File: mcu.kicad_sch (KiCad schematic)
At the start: 38 parts, among them IC14 W25Q64FWSSIG, IC19 TPS22975, IC3 HDC2080, IC5 CAT25160VI-GT3, J1 JST_PH_3PIN, J3 TC2030-IDC, J4 Conn_01x04, J6 Conn_01x08, J7 USB_C_Receptacle_USB2.0, SW1 SWITCH-SPST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

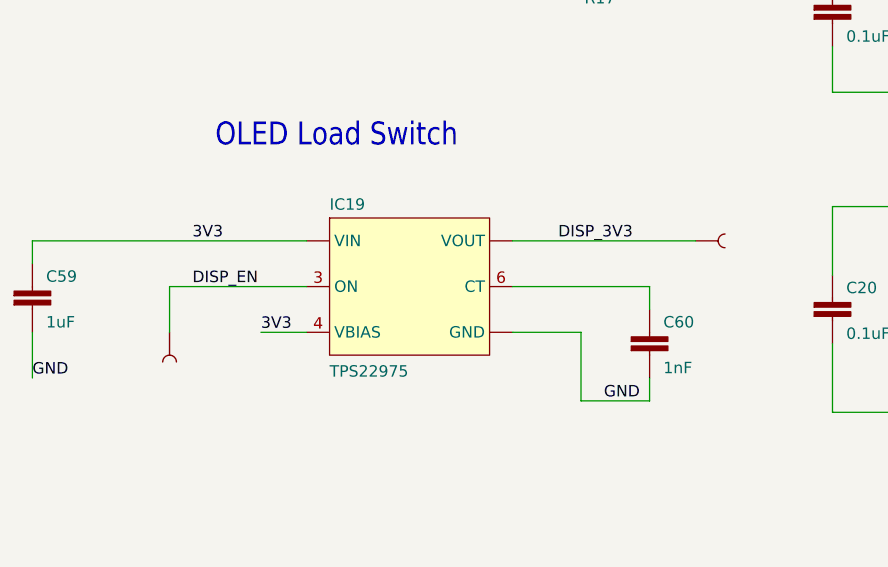
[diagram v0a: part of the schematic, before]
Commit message: name change to Loriques
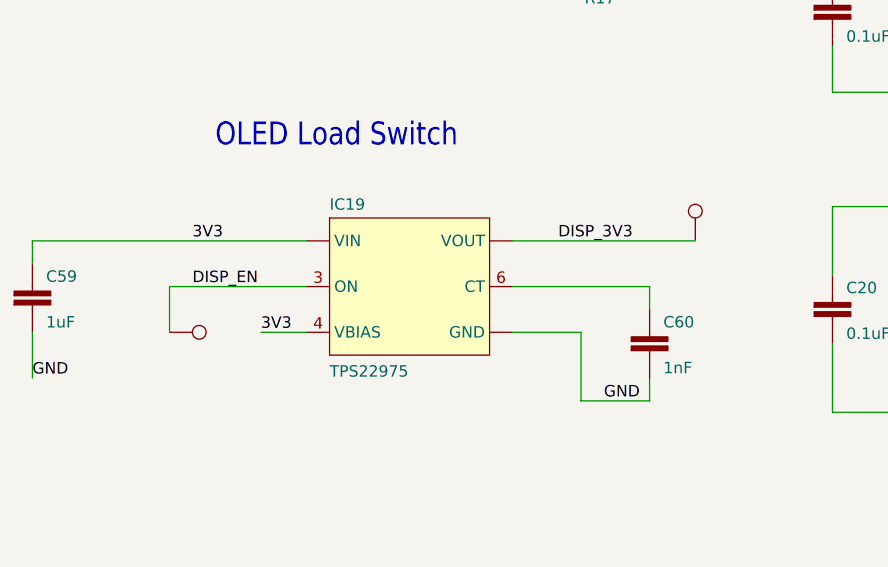
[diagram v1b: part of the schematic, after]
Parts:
- C20, C23, C59, C60, C9: symbol autonode:CAP0402 -> Loriques:CAP0402
- IC14: footprint autonode:SOIC127P790X216-8N -> Loriques:SOIC127P790X216-8N; symbol autonode:W25Q64FWSSIG -> Loriques:W25Q64FWSSIG
- IC19: footprint autonode:WSON8 -> Loriques:WSON8; symbol autonode:TPS22975 -> Loriques:TPS22975
- IC3: footprint autonode:DMB0006A -> Loriques:DMB0006A; symbol autonode:HDC2080 -> Loriques:HDC2080
- IC5: footprint autonode:SOIC127P600X175-8N -> Loriques:SOIC127P600X175-8N; symbol autonode:CAT25160VI-GT3 -> Loriques:CAT25160VI-GT3
- J1: footprint autonode:JST-PH-3-SMT -> Loriques:JST-PH-3-SMT
- J4: footprint autonode:PinHeader_1x04_P2.54mm_Vertical_shifted -> Loriques:PinHeader_1x04_P2.54mm_Vertical_shifted
- J6: footprint autonode:FPC-SMD_P0.50-8P_FGS-XJ-H2.0 -> Loriques:FPC-SMD_P0.50-8P_FGS-XJ-H2.0
- J7: footprint autonode:USB_C_Receptacle_GCT_USB4105-xx-A -> Loriques:USB_C_Receptacle_GCT_USB4105-xx-A
- LED0: footprint autonode:PLCC140P350X320X210-4 -> Loriques:PLCC140P350X320X210-4; symbol autonode:CLV1L-FKB -> Loriques:CLV1L-FKB
- R13, R16, R17, R22, R48, R49, R5: symbol autonode:RESISTOR0402-RES -> Loriques:RESISTOR0402-RES
- SW1, SW2: footprint autonode:SW_TL3330AF130QG_EWI -> Loriques:SW_TL3330AF130QG_EWI
- S_3V1, TP3: footprint autonode:PAD.03X.05 -> TestPoint:TestPoint_Pad_D1.5mm; symbol autonode:TEST-POINT3X5 -> Connector:TestPoint
- U1: footprint autonode:ESP32-S3-WROOM-1 -> Loriques:ESP32-S3-WROOM-1
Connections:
- net DISP_3V3: now also S_3V1.1; no longer S_3V1.0 (1)
- net DISP_EN: now also TP3.1; no longer TP3.0 (1)

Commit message: added logo to schematic sheets
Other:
- title: (none) -> Loriques
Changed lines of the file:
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@@
 	(generator "eeschema")
 	(generator_version "9.0")
-	(paper "User" 404.698 289.763)
+	(paper "A3")
+	(title_block
+		(title "Loriques")
+		(date "2025-07-11")
+		(rev "A")
+	)
 	(text "Temp/Humidity"
 		(exclude_from_sim no)

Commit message: added lots of 3d models
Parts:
- IC3: DK (none) -> 296-52638-1-ND; PARTNO (none) -> HDC2080DMBR
- J1: DK (none) -> 455-B3B-PH-SM4-TBCT-ND; PARTNO (none) -> B3B-PH-SM4-TB
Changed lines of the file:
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@@
+			)
+		)
+		(property "PARTNO" "HDC2080DMBR"
+			(at 82.55 38.1 0)
+			(effects
+				(font
+					(size 1.27 1.27)
+				)
+				(hide yes)
+			)
+		)
+		(property "DK" "296-52638-1-ND"
+			(at 82.55 38.1 0)
+			(effects
+				(font
+					(size 1.27 1.27)
+				)
+				(hide yes)
 			)
 		)
@@
 			(at 342.9 139.7 0)
 			(effects
+				(font
+					(size 1.27 1.27)
+				)
+				(hide yes)
+			)
+		)
+		(property "PARTNO" "B3B-PH-SM4-TB"
+			(at 342.9 139.7 0)
+			(effects
+				(font
+					(size 1.27 1.27)
+				)
+				(hide yes)
+			)
+		)
+		(property "DK" "455-B3B-PH-SM4-TBCT-ND"
+			(at 342.9 139.7 0)
+			(effects

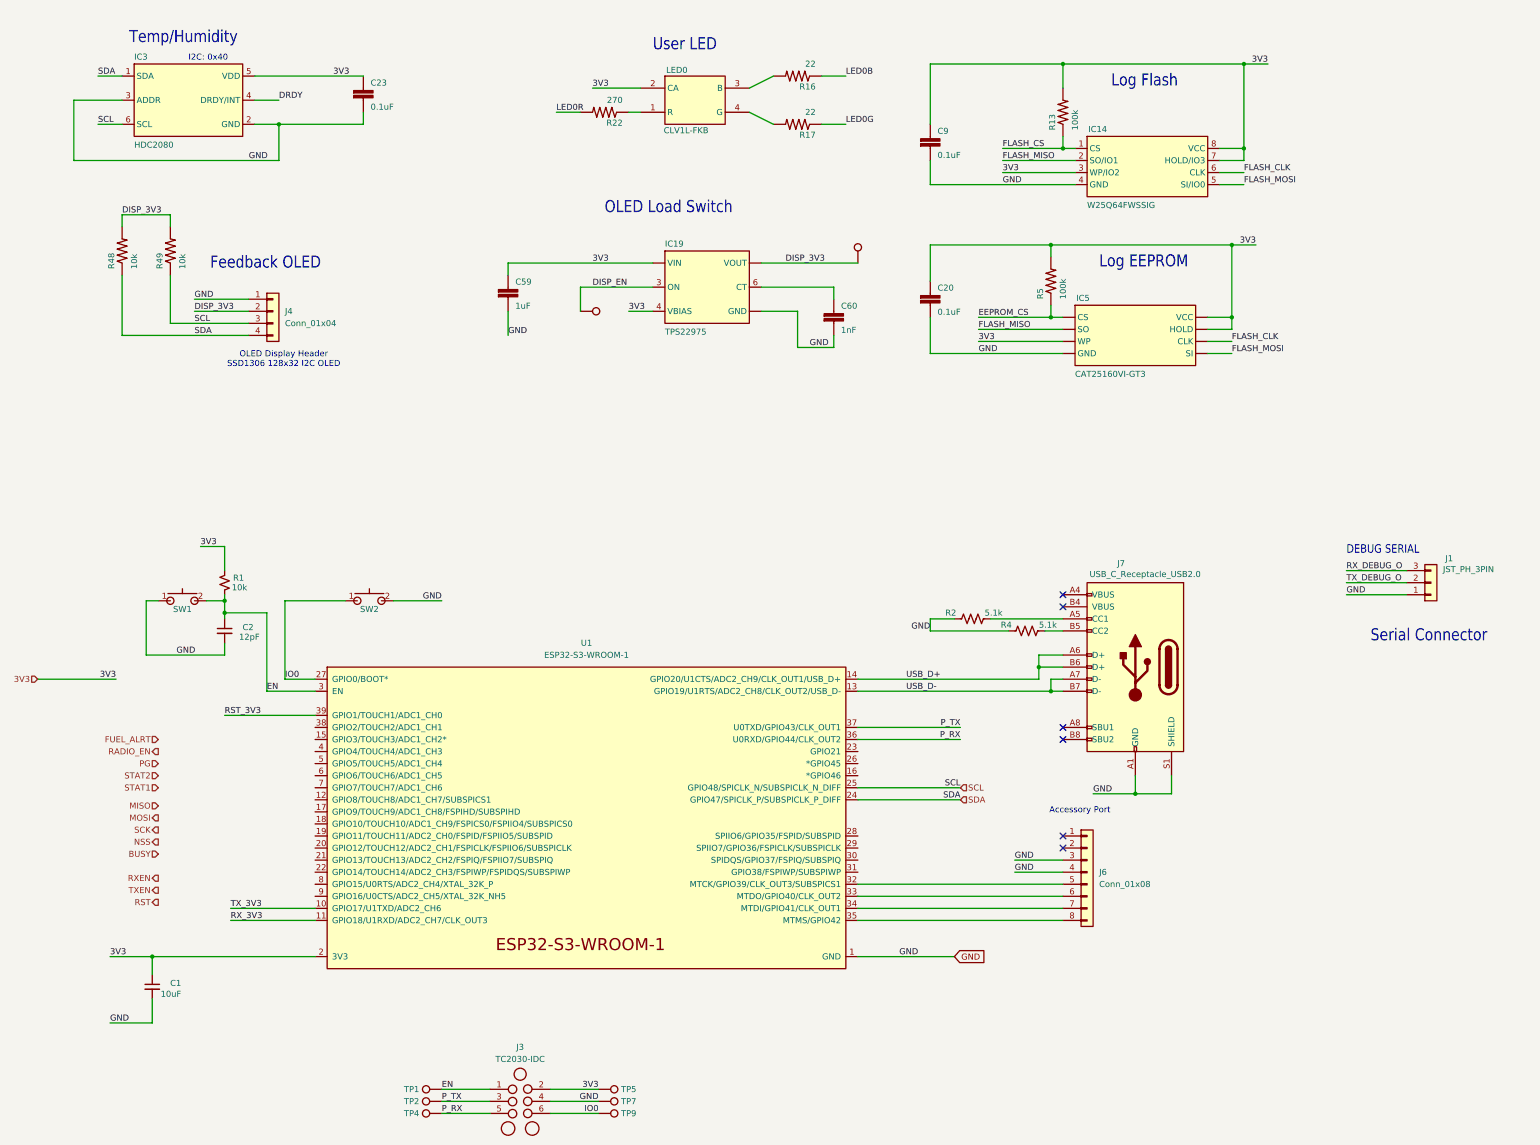
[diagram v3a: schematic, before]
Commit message: more 3D parts. changed out the temp/humidity sensor for an instock one
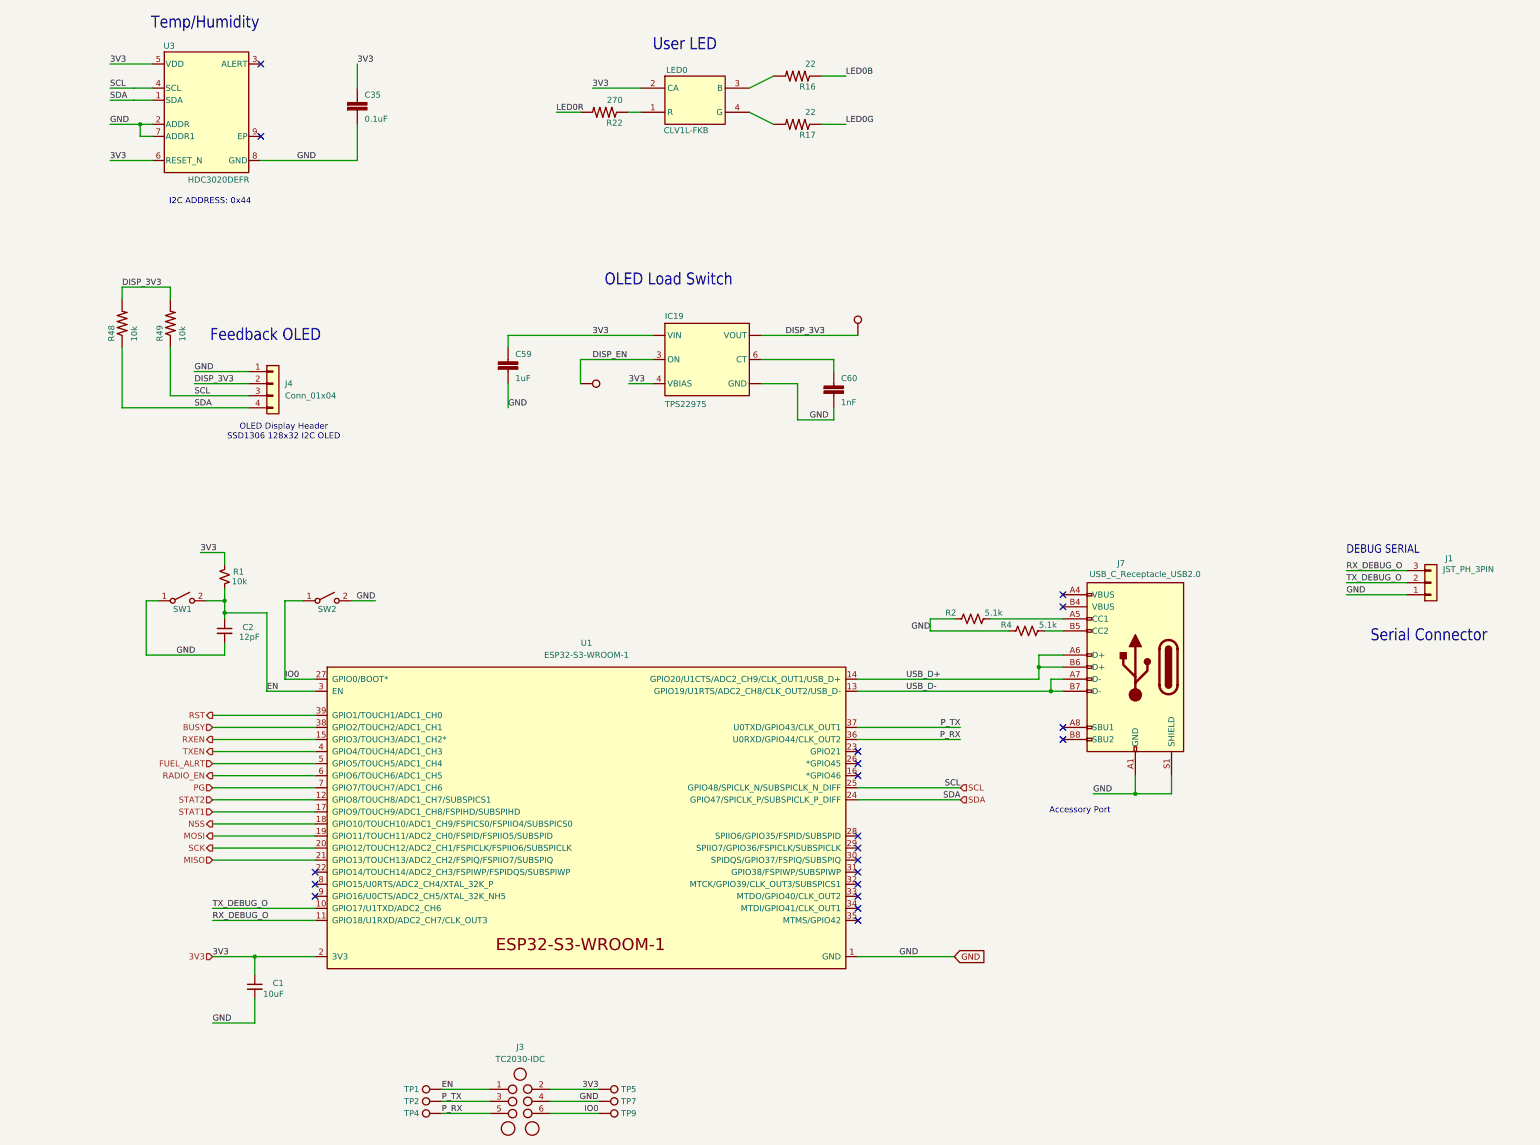
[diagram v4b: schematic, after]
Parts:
- removed C20, C23, C9: 0.1uF, Capacitor_SMD:C_0402_1005Metric, symbol Loriques:CAP0402
- removed IC14: W25Q64FWSSIG, Loriques:SOIC127P790X216-8N, symbol Loriques:W25Q64FWSSIG
- removed IC3: HDC2080, Loriques:DMB0006A, symbol Loriques:HDC2080
- removed IC5: CAT25160VI-GT3, Loriques:SOIC127P600X175-8N, symbol Loriques:CAT25160VI-GT3
- removed J6: Conn_01x08, Loriques:FPC-SMD_P0.50-8P_FGS-XJ-H2.0, symbol bitaxe:Conn_01x08-support
- removed R13, R5: 100k, Resistor_SMD:R_0402_1005Metric, symbol Loriques:RESISTOR0402-RES
- added C35: 0.1uF, Capacitor_SMD:C_0402_1005Metric, symbol Loriques:CAP0402
- added U3: HDC3020DEFR, Loriques:DEF0008A-IPC_A, symbol Loriques:HDC3020DEFR
- SW1: footprint Loriques:SW_TL3330AF130QG_EWI -> Loriques:SW_CS1213AGF260_CRS; symbol bitaxe:SWITCH-SPST -> Switch:SW_SPST; DK EG4388CT-ND -> 2449-CS1213AGF260CT-ND; LCSC (none) -> C5578986; PARTNO TL3330AF130QG -> CS1213AGF260
- SW2: footprint Loriques:SW_TL3330AF130QG_EWI -> Loriques:SW_CS1213AGF260_CRS; symbol bitaxe:SWITCH-SPST -> Switch:SW_SPST; DK EG4388CT-ND -> 2449-CS1213AGF260CT-ND; PARTNO TL3330AF130QG -> CS1213AGF260
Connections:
- net RST_3V3 is gone; now on net RST: U1.39 (GPIO1/TOUCH1/ADC1_CH0)
- net RX_3V3 is gone; now on net RX_DEBUG_O: U1.11 (GPIO18/U1RXD/ADC2_CH7/CLK_OUT3)
- net TX_3V3 is gone; now on net TX_DEBUG_O: U1.10 (GPIO17/U1TXD/ADC2_CH6)
- net 3V3: now also C35.1, U3.5 (VDD), U3.6 (RESET_N)
- net BUSY: now also U1.38 (GPIO2/TOUCH2/ADC1_CH1)
- net FUEL_ALRT: now also U1.5 (GPIO5/TOUCH5/ADC1_CH4)
- net GND: now also C35.2, U3.2 (ADDR), U3.7 (ADDR1), U3.8 (GND)
- net MISO: now also U1.21 (GPIO13/TOUCH13/ADC2_CH2/FSPIQ/FSPIIO7/SUBSPIQ)
- net MOSI: now also U1.19 (GPIO11/TOUCH11/ADC2_CH0/FSPID/FSPIIO5/SUBSPID)
- net NSS: now also U1.18 (GPIO10/TOUCH10/ADC1_CH9/FSPICS0/FSPIIO4/SUBSPICS0)
- net PG: now also U1.7 (GPIO7/TOUCH7/ADC1_CH6)
- net RADIO_EN: now also U1.6 (GPIO6/TOUCH6/ADC1_CH5)
- net RXEN: now also U1.15 (GPIO3/TOUCH3/ADC1_CH2*)
- net SCK: now also U1.20 (GPIO12/TOUCH12/ADC2_CH1/FSPICLK/FSPIIO6/SUBSPICLK)
- net SCL: now also U3.4 (SCL)
- net SDA: now also U3.1 (SDA)
- net STAT1: now also U1.17 (GPIO9/TOUCH9/ADC1_CH8/FSPIHD/SUBSPIHD)
- net STAT2: now also U1.12 (GPIO8/TOUCH8/ADC1_CH7/SUBSPICS1)
- net TXEN: now also U1.4 (GPIO4/TOUCH4/ADC1_CH3)
- no-connect marks 6 -> 20
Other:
- note added: "I2C ADDRESS: 0x44"
- note removed: "I2C: 0x40"
- note removed: "Log EEPROM"
- note removed: "Log Flash"
- moved on the sheet: C1, C59, C60, IC19, J4, R1, R48, R49

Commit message: lots of routing, tweaking placement. adding courtyards
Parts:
- IC19: DK (none) -> 296-47228-1-ND; PARTNO (none) -> TPS22975DSGR
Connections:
- net LED0B: now also U1.9 (GPIO16/U0CTS/ADC2_CH5/XTAL_32K_NH5)
- net LED0G: now also U1.8 (GPIO15/U0RTS/ADC2_CH4/XTAL_32K_P)
- net LED0R: now also U1.22 (GPIO14/TOUCH14/ADC2_CH3/FSPIWP/FSPIDQS/SUBSPIWP)
- no-connect marks 20 -> 17
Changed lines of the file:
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@@
 	)
 	(no_connect
-		(at 107.95 203.2)
-	)
-	(no_connect
 		(at 96.52 30.48)
 	)
@@
 	)
 	(no_connect
-		(at 107.95 205.74)
-	)
-	(no_connect
 		(at 265.43 170.18)
 	)
@@
 	)
 	(no_connect
-		(at 107.95 200.66)
-	)
-	(no_connect
 		(at 265.43 142.24)
 	)
@@
 	(wire
 		(pts
+			(xy 86.36 200.66) (xy 107.95 200.66)
+		)
+		(stroke
+			(width 0)
+			(type default)
+		)
+	)
+	(wire
+		(pts
 			(xy 222.25 170.18) (xy 243.84 170.18)
 		)
@@
 	(wire
 		(pts
+			(xy 86.36 205.74) (xy 107.95 205.74)
+		)
+		(stroke
+			(width 0)
+			(type default)
+		)
+	)
+	(wire
+		(pts
 			(xy 86.36 182.88) (xy 107.95 182.88)
 		)
@@
 	(wire
 		(pts
+			(xy 86.36 203.2) (xy 107.95 203.2)
+		)
+		(stroke
+			(width 0)
+			(type default)
+		)
+	)
+	(wire
+		(pts
 			(xy 86.36 170.18) (xy 107.95 170.18)
 		)
@@
 		)
 	)
+	(label "LED0R"
+		(at 86.36 200.66 0)
+		(effects
+			(font
+				(size 1.27 1.27)
+			)
+			(justify left bottom)
+		)
+	)
 	(label "3V3"
 		(at 64.77 30.48 0)
@@
 		)
 	)
+	(label "LED0G"
+		(at 86.36 203.2 0)
+		(effects
+			(font
+				(size 1.27 1.27)
+			)
+			(justify left bottom)
+		)
+	)
 	(label "GND"
 		(at 82.55 95.25 0)
@@
 		)
 	)
+	(label "LED0B"
+		(at 86.36 205.74 0)
+		(effects
+			(font
+				(size 1.27 1.27)
+			)
+			(justify left bottom)
+		)
+	)
 	(label "LED0G"
 		(at 219.71 43.18 0)
@@
 			)
 		)
-		(property "Datasheet" ""
+		(property "Datasheet" "https://www.ti.com/lit/ds/symlink/tps22975.pdf"
 			(at 189.23 92.71 0)
 			(effects
@@
 			)
 		)
-		(property "Description" "TPS22975\nLOAD SWITCH N-CH 6A 8WSON"
+		(property "Description" "LOAD SWITCH N-CH 6A 8WSON"
 			(at 189.23 92.71 0)
 			(effects
 				(font
+					(size 1.27 1.27)
+				)
+				(hide yes)
+			)
+		)
+		(property "PARTNO" "TPS22975DSGR"
+			(at 189.23 105.918 0)
+			(effects
+				(font
+					(size 1.27 1.27)
+				)
+				(hide yes)
+			)
+		)
+		(property "DK" "296-47228-1-ND"
+			(at 189.23 105.918 0)
+			(effects
+				(font

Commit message: initial routing done!
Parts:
- J7: footprint Loriques:USB_C_Receptacle_GCT_USB4105-xx-A -> Loriques:CONN_12402032E202A_AMP; DK 2073-USB4105-GF-ACT-ND -> 664-12402032E202ACT-ND; PARTNO USB4105-GF-A -> 12402032E202A
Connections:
- net DISP_EN: now also U1.23 (GPIO21)
- no-connect marks 17 -> 16
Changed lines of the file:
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@@
-	)
-	(no_connect
-		(at 222.25 175.26)
 	)
 	(no_connect
@@
 	(wire
 		(pts
+			(xy 222.25 175.26) (xy 243.84 175.26)
+		)
+		(stroke
+			(width 0)
+			(type default)
+		)
+	)
+	(wire
+		(pts
 			(xy 179.07 97.79) (xy 173.99 97.79)
 		)
@@
 			)
 			(justify left bottom)
+		)
+	)
+	(label "DISP_EN"
+		(at 243.84 175.26 180)
+		(effects
+			(font
+				(size 1.27 1.27)
+			)
+			(justify right bottom)
 		)
 	)
@@
 			)
 		)
-		(property "Footprint" "Loriques:USB_C_Receptacle_GCT_USB4105-xx-A"
+		(property "Footprint" "Loriques:CONN_12402032E202A_AMP"
 			(at 276.86 157.48 0)
 			(effects
@@
 			)
 		)
-		(property "Datasheet" "https://www.usb.org/sites/default/files/documents/usb_type-c.zip"
+		(property "Datasheet" "https://mm.digikey.com/Volume0/opasdata/d220001/medias/docus/2614/C12402032-3.pdf"
 			(at 278.13 134.62 0)
 			(effects
@@
 			)
 		)
-		(property "DK" "2073-USB4105-GF-ACT-ND"
+		(property "DK" "664-12402032E202ACT-ND"
 			(at 280.67 157.48 0)
 			(effects
@@
 			)
 		)
-		(property "PARTNO" "USB4105-GF-A"
+		(property "PARTNO" "12402032E202A"
 			(at 280.67 157.48 0)
 			(effects

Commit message: some DRC fixing
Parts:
- removed J1: JST_PH_3PIN, Loriques:JST-PH-3-SMT, symbol Connector_Generic:Conn_01x03
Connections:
- net RX_DEBUG_O: no longer names the net of U1.11 (GPIO18/U1RXD/ADC2_CH7/CLK_OUT3)
- net TX_DEBUG_O: no longer names the net of U1.10 (GPIO17/U1TXD/ADC2_CH6)
- no-connect marks 16 -> 18
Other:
- note removed: "DEBUG SERIAL"
- note removed: "Serial Connector"
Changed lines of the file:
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@@
 		)
 	)
-	(text "Serial Connector"
-		(exclude_from_sim no)
-		(at 330.2 152.4 0)
-		(effects
-			(font
-				(size 2.54 2.159)
-			)
-			(justify left bottom)
-		)
-	)
 	(text "OLED Load Switch"
 		(exclude_from_sim no)
@@
 		)
 	)
-	(text "DEBUG SERIAL"
-		(exclude_from_sim no)
-		(at 325.12 133.858 0)
-		(effects
-			(font
-				(size 1.778 1.5113)
-			)
-			(justify left bottom)
-		)
-	)
 	(text "User LED\n"
 		(exclude_from_sim no)
@@
 	)
 	(no_connect
+		(at 107.95 210.82)
+	)
+	(no_connect
 		(at 96.52 30.48)
 	)
 	(no_connect
+		(at 107.95 208.28)
+	)
+	(no_connect
 		(at 96.52 45.72)
 	)
@@
 	(wire
 		(pts
-			(xy 337.82 142.24) (xy 325.12 142.24)
-		)
-		(stroke
-			(width 0.1524)
-			(type solid)
-		)
-	)
-	(wire
-		(pts
 			(xy 262.89 162.56) (xy 265.43 162.56)
 		)
@@
 	(wire
 		(pts
-			(xy 86.36 210.82) (xy 107.95 210.82)
-		)
-		(stroke
-			(width 0)
-			(type default)
-		)
-	)
-	(wire
-		(pts
 			(xy 83.82 133.35) (xy 88.9 133.35)
 		)
@@
 	(wire
 		(pts
-			(xy 86.36 208.28) (xy 107.95 208.28)
-		)
-		(stroke
-			(width 0)
-			(type default)
-		)
-	)
-	(wire
-		(pts
 			(xy 222.25 185.42) (xy 243.84 185.42)
 		)
@@
 	(wire
 		(pts
-			(xy 325.12 137.16) (xy 337.82 137.16)
-		)
-		(stroke
-			(width 0.1524)
-			(type solid)
-		)
-	)
-	(wire
-		(pts
 			(xy 72.39 154.94) (xy 88.9 154.94)
 		)
@@
 	(wire
 		(pts
-			(xy 337.82 139.7) (xy 325.12 139.7)
-		)
-		(stroke
-			(width 0.1524)
-			(type solid)
-		)
-	)
-	(wire
-		(pts
 			(xy 69.85 35.56) (xy 64.77 35.56)
 		)
@@
 		)
 	)
-	(label "GND"
-		(at 325.12 142.24 0)
-		(effects
-			(font
-				(size 1.27 1.27)
-			)
-			(justify left bottom)
-		)
-	)
 	(label "SDA"
 		(at 64.77 38.1 0)
@@
 		)
 	)
-	(label "RX_DEBUG_O"
-		(at 325.12 137.16 0)
-		(effects
-			(font
-				(size 1.27 1.27)
-			)
-			(justify left bottom)
-		)
-	)
 	(label "SCL"
 		(at 243.84 182.88 180)
@@
 		)
 	)
-	(label "RX_DEBUG_O"
-		(at 86.36 210.82 0)
-		(effects
-			(font
-				(size 1.27 1.27)
-			)
-			(justify left bottom)
-		)
-	)
 	(label "LED0G"
 		(at 86.36 203.2 0)
@@
 		)
 	)
-	(label "TX_DEBUG_O"
-		(at 325.12 139.7 0)
-		(effects
-			(font
-				(size 1.27 1.27)
-			)
-			(justify left bottom)
-		)
-	)
 	(label "GND"
 		(at 212.09 105.41 0)
@@
 		)
 	)
-	(label "TX_DEBUG_O"
-		(at 86.36 208.28 0)
-		(effects
-			(font
-				(size 1.27 1.27)
-			)
-			(justify left bottom)
-		)
-	)
 	(label "GND"
 		(at 148.59 102.87 0)
@@
 					(unit 1)
 				)
-			)
-		)
-	)
-	(symbol
-		(lib_id "Connector_Generic:Conn_01x03")
-		(at 342.9 139.7 0)
-		(mirror x)
-		(unit 1)
-		(exclude_from_sim no)
-		(in_bom yes)
-		(on_board yes)
-		(dnp no)
-		(property "Reference" "J1"
-			(at 345.948 133.858 0)
-			(effects
-				(font
-					(size 1.27 1.27)
-				)
-				(justify left bottom)
-			)
-		)
-		(property "Value" "JST_PH_3PIN"
-			(at 345.44 136.144 0)
-			(effects
-				(font
-					(size 1.27 1.27)
-				)
-				(justify left bottom)
-			)
-		)
-		(property "Footprint" "Loriques:JST-PH-3-SMT"
-			(at 342.9 139.7 0)
-			(effects
-				(font
-					(size 1.27 1.27)
-				)
-				(hide yes)
-			)
-		)
-		(property "Datasheet" "~"
-			(at 342.9 139.7 0)
-			(effects
-				(font
-					(size 1.27 1.27)
-				)
-				(hide yes)
-			)
-		)
-		(property "Description" "Generic connector, single row, 01x03, script generated (kicad-library-utils/schlib/autogen/connector/)"
-			(at 342.9 139.7 0)
-			(effects
-				(font
-					(size 1.27 1.27)
-				)
-				(hide yes)
-			)
-		)
-		(property "PARTNO" "B3B-PH-SM4-TB"
-			(at 342.9 139.7 0)
-			(effects
-				(font
-					(size 1.27 1.27)
-				)
-				(hide yes)
-			)
-		)
-		(property "DK" "455-B3B-PH-SM4-TBCT-ND"
-			(at 342.9 139.7 0)
-			(effects
-				(font
-					(size 1.27 1.27)
-				)
-				(hide yes)
-			)
-		)
-		(pin "1"
-		)
-		(pin "2"
-		)
-		(pin "3"
-		)
-		(instances
-			(project "Loriques"
-				(path "/23714a9e-6212-41ed-9d80-e983f828d45f/02db5e49-999f-43d3-aed1-3a2dd3ad0a6f"
-					(reference "J1")
-					(unit 1)
-				)
